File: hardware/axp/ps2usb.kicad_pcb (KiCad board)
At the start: 2 copper layers, 40 x 55 mm, 22 parts, among them J1 DIN8, J2 USB1035, J3 DIN8, J4 DB9_Female_MountingHoles, J5 Conn_01x03_Pin, U1 CH559L-less, U2 MAX232

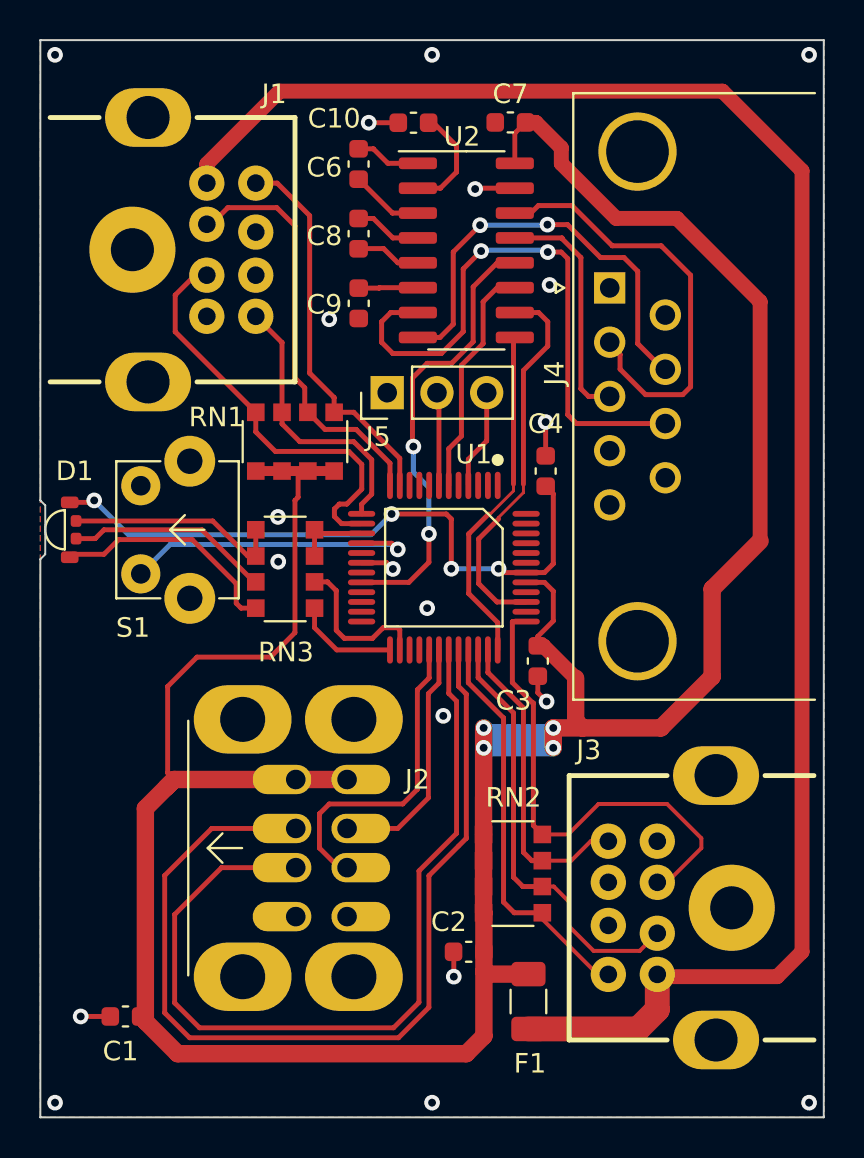
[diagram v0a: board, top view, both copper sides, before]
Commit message: Added crystal to PCB
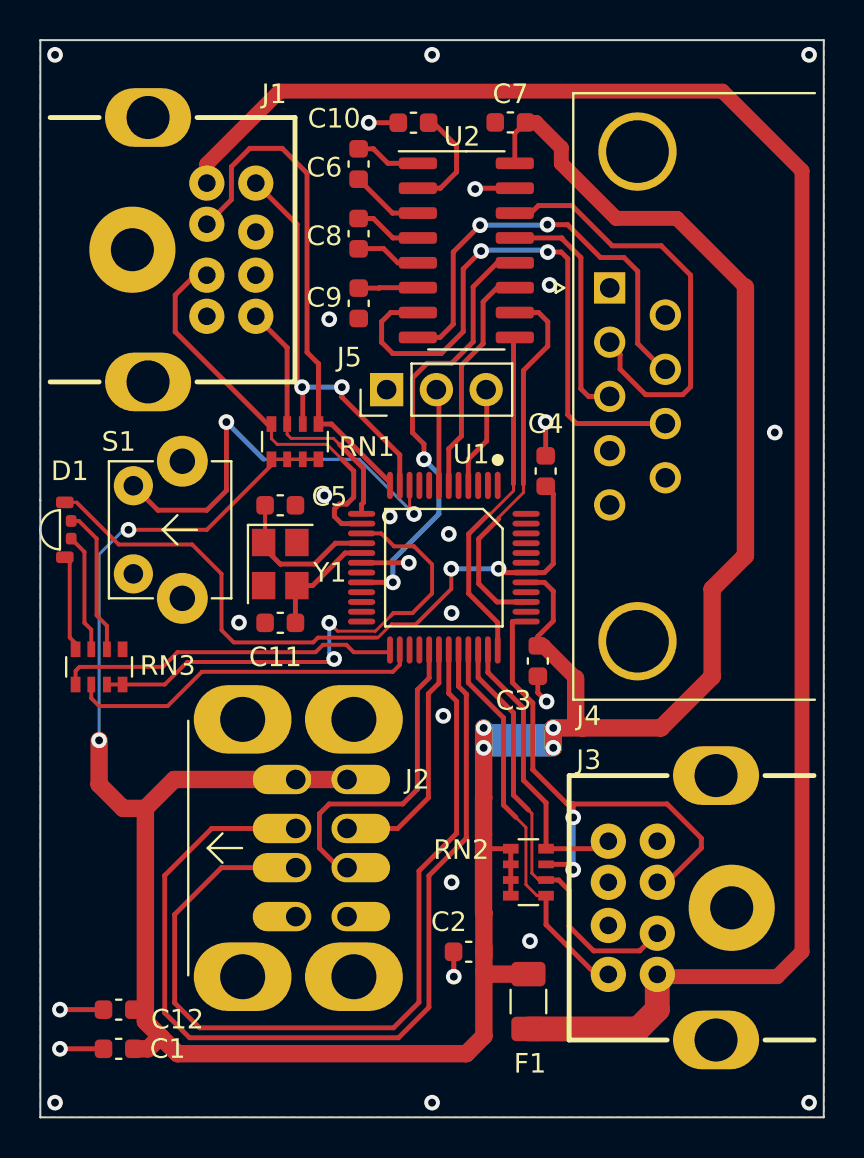
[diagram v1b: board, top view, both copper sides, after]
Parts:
- added C11: 10pF, Capacitor_SMD:C_0603_1608Metric, F.Cu at (109.2, 97.2)
- added C12: 3.3u, Capacitor_SMD:C_0603_1608Metric, F.Cu at (101.0, 119.0)
- added C5: 10pF, Capacitor_SMD:C_0603_1608Metric, F.Cu at (109.2, 91.2)
- added Y1: 12MHz, Crystal:Crystal_SMD_3225-4Pin_3.2x2.5mm, F.Cu at (109.2, 94.2)
- C10, C6, C7, C8, C9: value 1u -> 3.3u
- C3: value 100n -> 3.3u
- J4: value DB9_Female_MountingHoles -> DE9
- RN1, RN2, RN3: footprint Resistor_SMD:R_Array_Convex_4x1206 -> Resistor_SMD:R_Array_Convex_4x0603
- moved RN3 10.7 mm to (100.0, 99.5), turned to -90 degrees
- moved RN2 0.79 mm to (121.9, 110.0)
- moved C1 0.49 mm to (101.0, 117.0)
- moved S1 0.38 mm to (103.0, 92.5)
- moved D1 0.25 mm to (98.2, 92.5)
- moved J5 0.16 mm to (114.7, 85.3)
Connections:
- RN1 pad 1: /DIN1-8 -> /DIN1-2
- RN1 pad 2: /DIN1-2 -> /DIN1-8
- RN2 pad 3: /DIN2-6 -> /DIN2-1
- RN2 pad 4: /DIN2-1 -> /DIN2-6
- S1 pad 1: GND -> Net-(U1A-P3.4/LEDC/XCS0/T0)
- S1 pad 2: Net-(U1A-P4.6/XI/SCS_) -> GND
- U1 pad 10: (no net) -> Net-(U1A-P3.4/LEDC/XCS0/T0)
- U1 pad 17: (no net) -> Net-(U1A-P4.7/X0/SCK_)
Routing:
- net Net-(RN3-R1.2): track 3.99 -> 26.4 mm, vias 0 -> 2
- net Net-(U1A-P3.4/LEDC/XCS0/T0): track 0.00 -> 22.4 mm, vias 0 -> 2
- net Net-(RN3-R4.2): track 5.32 -> 17.3 mm
- net Net-(RN3-R3.2): track 8.03 -> 18.3 mm
- net Net-(U1A-P4.6/XI/SCS_): track 15.8 -> 7.98 mm, vias 1 -> 0
- net +5V: track 149.9 -> 157.2 mm, vias 4 -> 6
- net Net-(D1-R): track 11.9 -> 4.93 mm
- net Net-(U1A-P4.7/X0/SCK_): track 0.00 -> 5.92 mm
- net /DIN1-2: track 21.4 -> 26.5 mm
- net Net-(D1-G): track 10.5 -> 6.07 mm
- net Net-(D1-B): track 11.3 -> 7.54 mm
- net GND: track 12.8 -> 16.5 mm, vias 19 -> 25
- net +3.3V: track 32.9 -> 36.1 mm, vias 4 -> 2
- net /DIN2-1: track 25.2 -> 27.1 mm, vias 0 -> 2
- net /DIN1-8: track 19.7 -> 21.6 mm, vias 0 -> 2
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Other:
- outline, holes or cut-outs redrawn
- board text added: "AXP"
- board text added: "github:rasteri/HIDman"
- board text added: "rev c"
- board text removed: "rasteri.com"

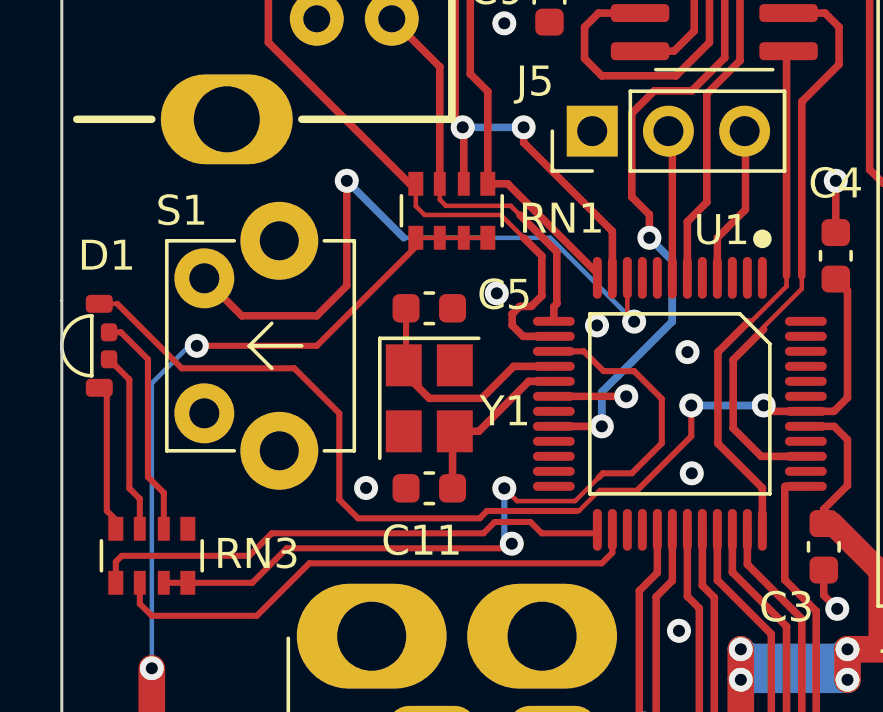
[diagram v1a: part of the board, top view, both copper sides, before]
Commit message: Software for new switch pin, refactoring, latest gerbers,
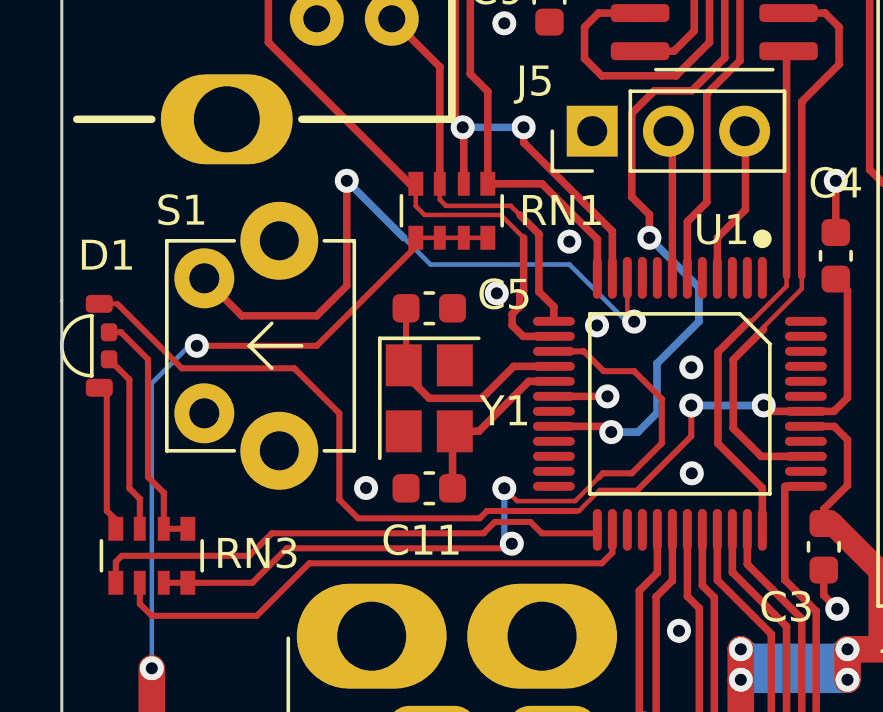
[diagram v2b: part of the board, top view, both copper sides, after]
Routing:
- net Net-(U1A-P4.0/LED2/A0/RXD1_): track 22.9 -> 24.6 mm
- net Net-(D1-B): track 7.54 -> 8.34 mm
- net /DIN1-1: track 21.3 -> 20.6 mm
- net /DIN1-2: track 26.5 -> 27.2 mm
- net GND: track 16.5 -> 15.9 mm, vias 25 -> 26
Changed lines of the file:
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@@
 		(tags "resistor array")
 		(property "Reference" "RN1"
-			(at 0.265 -3.665 0)
+			(at 0.011 -3.665 0)
 			(layer "F.SilkS")
 			(effects
@@
 	)
 	(segment
+		(start 115.189 94.185)
+		(end 113.402 94.185)
+		(width 0.25)
+		(layer "F.Cu")
+		(net 2)
+	)
+	(segment
 		(start 122.4 100.819142)
 		(end 122.4 99.975)
@@
 	)
 	(segment
-		(start 115.815 94.185)
-		(end 113.402 94.185)
-		(width 0.25)
-		(layer "F.Cu")
-		(net 2)
-	)
-	(segment
 		(start 118.097 115.329)
 		(end 118.11 115.316)
@@
 	)
 	(via
+		(at 113.919 89.027)
+		(size 0.8)
+		(drill 0.4)
+		(layers "F.Cu" "B.Cu")
+		(free yes)
+		(net 2)
+	)
+	(via
 		(at 122.848345 101.267487)
 		(size 0.8)
@@
 	)
 	(via
-		(at 117.856 92.71)
+		(at 117.983 93.218)
 		(size 0.8)
 		(drill 0.4)
@@
 	)
 	(via
-		(at 115.815 94.185)
+		(at 115.189 94.185)
 		(size 0.8)
 		(drill 0.4)
@@
 	)
 	(segment
-		(start 112.268 91.186)
-		(end 112.014 91.44)
+		(start 112.014 91.821)
+		(end 112.378 92.185)
 		(width 0.254)
 		(layer "F.Cu")
@@
 	)
 	(segment
-		(start 112.395 88.9)
-		(end 113 89.505)
+		(start 108.597326 87.1)
+		(end 108.8 87.1)
 		(width 0.254)
 		(layer "F.Cu")
@@
 	)
 	(segment
-		(start 113 89.505)
-		(end 113 90.835)
+		(start 112.014 91.44)
+		(end 112.014 91.821)
 		(width 0.254)
 		(layer "F.Cu")
@@
 	)
 	(segment
-		(start 112.649 91.186)
-		(end 112.268 91.186)
+		(start 112.268 91.186)
+		(end 112.014 91.44)
 		(width 0.254)
 		(layer "F.Cu")
@@
 	)
 	(segment
-		(start 108.597326 87.1)
-		(end 108.8 87.1)
+		(start 105.5625 78.8)
+		(end 105.14 78.8)
 		(width 0.254)
 		(layer "F.Cu")
@@
 	)
 	(segment
-		(start 105.5625 78.8)
-		(end 105.14 78.8)
+		(start 112.395 88.9)
+		(end 112.395 90.678)
 		(width 0.254)
 		(layer "F.Cu")
@@
 	)
 	(segment
-		(start 112.014 91.44)
-		(end 112.014 91.821)
-		(width 0.254)
+		(start 112.395 88.9)
+		(end 111.633 88.138)
+		(width 0.1524)
 		(layer "F.Cu")
 		(net 4)
 	)
 	(segment
-		(start 112.378 92.185)
-		(end 113.402 92.185)
+		(start 104.904 79.5)
+		(end 103.886 80.518)
 		(width 0.254)
 		(layer "F.Cu")
@@
 	)
 	(segment
-		(start 112.395 88.9)
-		(end 111.633 88.138)
-		(width 0.1524)
+		(start 112.395 90.678)
+		(end 112.268 90.805)
+		(width 0.254)
 		(layer "F.Cu")
 		(net 4)
 	)
 	(segment
-		(start 104.904 79.5)
-		(end 103.886 80.518)
+		(start 112.378 92.185)
+		(end 113.402 92.185)
 		(width 0.254)
 		(layer "F.Cu")
@@
 	)
 	(segment
-		(start 113 90.835)
-		(end 112.649 91.186)
+		(start 112.268 90.805)
+		(end 112.268 91.186)
 		(width 0.254)
 		(layer "F.Cu")
@@
 	)
 	(segment
-		(start 112.014 91.821)
-		(end 112.378 92.185)
-		(width 0.254)
-		(layer "F.Cu")
-		(net 4)
-	)
-	(segment
 		(start 106.755785 75.644215)
 		(end 105.5 76.9)
@@
 	)
 	(segment
+		(start 114.852 90.235)
+		(end 114.852 88.944)
+		(width 0.254)
+		(layer "F.Cu")
+		(net 5)
+	)
+	(segment
 		(start 110.617 83.439)
 		(end 110.617 74.295)
@@
 	)
 	(segment
-		(start 114.852 90.087)
-		(end 111.865 87.1)
+		(start 113.008 87.1)
+		(end 111.2 87.1)
 		(width 0.254)
 		(layer "F.Cu")
@@
 	)
 	(segment
-		(start 106.755785 73.965215)
-		(end 106.755785 75.644215)
+		(start 114.852 88.944)
+		(end 113.008 87.1)
 		(width 0.254)
 		(layer "F.Cu")
@@
 	)
 	(segment
-		(start 111.865 87.1)
-		(end 111.2 87.1)
+		(start 106.755785 73.965215)
+		(end 106.755785 75.644215)
 		(width 0.254)
 		(layer "F.Cu")
@@
 	)
 	(segment
-		(start 114.852 90.235)
-		(end 114.852 90.087)
+		(start 113.402 91.195)
+		(end 113.402 91.685)
 		(width 0.254)
 		(layer "F.Cu")
-		(net 5)
+		(net 6)
 	)
 	(segment
@@
 	)
 	(segment
-		(start 113.5 91.097)
-		(end 113.402 91.195)
+		(start 112.268 88.138)
+		(end 112.903 88.773)
 		(width 0.254)
 		(layer "F.Cu")
@@
 	)
 	(segment
-		(start 112.268 88.138)
-		(end 113.5 89.37)
-		(width 0.254)
-		(layer "F.Cu")
-		(net 6)
-	)
-	(segment
-		(start 113.5 89.37)
-		(end 113.5 91.097)
+		(start 109.6 83.2)
+		(end 108 81.6)
 		(width 0.254)
 		(layer "F.Cu")
@@
 	)
 	(segment
-		(start 109.6 83.2)
-		(end 108 81.6)
+		(start 112.903 90.696)
+		(end 113.402 91.195)
 		(width 0.254)
 		(layer "F.Cu")
@@
 	)
 	(segment
-		(start 113.402 91.195)
-		(end 113.402 91.685)
+		(start 109.6 87.1)
+		(end 109.6 83.2)
 		(width 0.254)
 		(layer "F.Cu")
@@
 	)
 	(segment
-		(start 109.6 87.1)
-		(end 109.6 83.2)
+		(start 112.903 88.773)
+		(end 112.903 90.696)
 		(width 0.254)
 		(layer "F.Cu")
@@
 	)
 	(segment
+		(start 100.4 98.6)
+		(end 101.2 98.6)
+		(width 0.2032)
+		(layer "F.Cu")
+		(net 22)
+	)
+	(segment
 		(start 99.25248 97.25248)
 		(end 99.25248 93.62748)
@@
 	)
 	(segment
-		(start 115 95.185)
-		(end 113.402 95.185)
+		(start 116.586 88.125183)
+		(end 116 87.539183)
 		(width 0.254)
 		(layer "F.Cu")
@@
 	)
 	(segment
-		(start 116.586 88.125183)
-		(end 116 87.539183)
+		(start 116 87.539183)
+		(end 116 84.75)
 		(width 0.254)
 		(layer "F.Cu")
@@
 	)
 	(segment
-		(start 116 87.539183)
-		(end 116 84.75)
+		(start 115.316 95.377)
+		(end 115.124 95.185)
 		(width 0.254)
 		(layer "F.Cu")
@@
 	)
 	(segment
+		(start 115.124 95.185)
+		(end 113.402 95.185)
+		(width 0.254)
+		(layer "F.Cu")
+		(net 44)
+	)
+	(segment
 		(start 119.098 82.902)
 		(end 119.098 80.0978)
@@
 	)
 	(via
-		(at 115 95.185)
+		(at 115.316 95.377)
 		(size 0.8)
 		(drill 0.4)
@@
 	)
 	(segment
-		(start 115 94.039183)
-		(end 115 95.185)
+		(start 116.205 95.377)
+		(end 116.84 94.742)
 		(width 0.254)
 		(layer "B.Cu")
@@
 	)
 	(segment
-		(start 117.348 91.694)
-		(end 115.5364 93.5056)
+		(start 118.237 90.551)
+		(end 116.586 88.9)
 		(width 0.254)
 		(layer "B.Cu")
@@
 	)
 	(segment
-		(start 115.5364 93.5056)
-		(end 115.533583 93.5056)
+		(start 116.84 94.742)
+		(end 116.84 93.091)
 		(width 0.254)
 		(layer "B.Cu")
@@
 	)
 	(segment
-		(start 117.348 89.662)
-		(end 117.348 91.694)
+		(start 116.84 93.091)
+		(end 118.237 91.694)
 		(width 0.254)
 		(layer "B.Cu")
@@
 	)
 	(segment
-		(start 115.533583 93.5056)
-		(end 115 94.039183)
+		(start 115.316 95.377)
+		(end 116.205 95.377)
 		(width 0.254)
 		(layer "B.Cu")
@@
 	)
 	(segment
-		(start 116.586 88.9)
-		(end 117.348 89.662)
+		(start 118.237 91.694)
+		(end 118.237 90.551)
 		(width 0.254)
 		(layer "B.Cu")
@@
 	)
 	(segment
+		(start 113.919 89.789)
+		(end 115.824 91.694)
+		(width 0.1524)
+		(layer "B.Cu")
+		(net 49)
+	)
+	(segment
 		(start 108.4 88.9)
-		(end 113.284 88.9)
+		(end 106.5 87)
+		(width 0.25)
+		(layer "B.Cu")
+		(net 49)
+	)
+	(segment
+		(start 108.4 88.9)
+		(end 109.289 89.789)
 		(width 0.1524)
 		(layer "B.Cu")
@@
 	)
 	(segment
-		(start 113.284 88.9)
-		(end 116.078 91.694)
+		(start 109.289 89.789)
+		(end 113.919 89.789)
 		(width 0.1524)
 		(layer "B.Cu")
@@
 	)
 	(segment
-		(start 108.4 88.9)
-		(end 106.5 87)
-		(width 0.25)
+		(start 115.824 91.694)
+		(end 116.078 91.694)
+		(width 0.1524)
 		(layer "B.Cu")
 		(net 49)

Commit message: redundant code cleanup
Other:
- board text added: "rev d"
- board text removed: "rev c"
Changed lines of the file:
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@@
 		(at 98.25 92.5 180)
 		(property "Reference" "D1"
-			(at -0.25 3 0)
+			(at -0.25 -3 0)
 			(unlocked yes)
 			(layer "F.SilkS")
@@
 		)
 		(property "Value" "Conn_01x03_Pin"
-			(at 0 7.41 270)
+			(at 0 7.41 -90)
 			(layer "F.Fab")
 			(effects
@@
 		)
 		(fp_text user "${REFERENCE}"
-			(at 0 2.54 360)
+			(at 0 2.54 0)
 			(layer "F.Fab")
 			(effects
@@
 		(layer "B.SilkS")
 	)
+	(gr_circle
+		(center 99.271176 91.183159)
+		(end 99.424647 91.233822)
+		(stroke
+			(width 0.3)
+			(type default)
+		)
+		(fill none)
+		(layer "F.SilkS")
+	)
 	(gr_poly
 		(pts
@@
 		)
 	)
-	(gr_text "rev c"
+	(gr_text "rev d"
 		(at 118 79.5 0)
 		(layer "B.SilkS")
@@
 	)
 	(segment
-		(start 130.75 108.75)
-		(end 129 110.5)
+		(start 124.206 107.188)
+		(end 124.206 106.5)
 		(width 0.254)
 		(layer "F.Cu")
@@
 	)
 	(segment
-		(start 124.206 107.188)
-		(end 124.206 106.5)
+		(start 130.5 108)
+		(end 130.5 109)
 		(width 0.254)
 		(layer "F.Cu")
@@
 	)
 	(segment
-		(start 121.1 100.3)
-		(end 122.146 101.346)
+		(start 129 106.5)
+		(end 130.5 108)
 		(width 0.254)
 		(layer "F.Cu")
@@
 	)
 	(segment
-		(start 124.206 106.5)
-		(end 129 106.5)
+		(start 121.1 100.3)
+		(end 122.146 101.346)
 		(width 0.254)
 		(layer "F.Cu")
@@
 	)
 	(segment
-		(start 130.75 108.25)
-		(end 130.75 108.75)
+		(start 124.206 106.5)
+		(end 129 106.5)
 		(width 0.254)
 		(layer "F.Cu")
@@
 	)
 	(segment
+		(start 130.5 109)
+		(end 129 110.5)
+		(width 0.254)
+		(layer "F.Cu")
+		(net 8)
+	)
+	(segment
 		(start 121.802 97.185)
 		(end 121.115 97.185)
@@
 		(width 0.254)
 		(layer "F.Cu")
-		(net 8)
-	)
-	(segment
-		(start 129 106.5)
-		(end 130.75 108.25)
-		(width 0.254)
-		(layer "F.Cu")

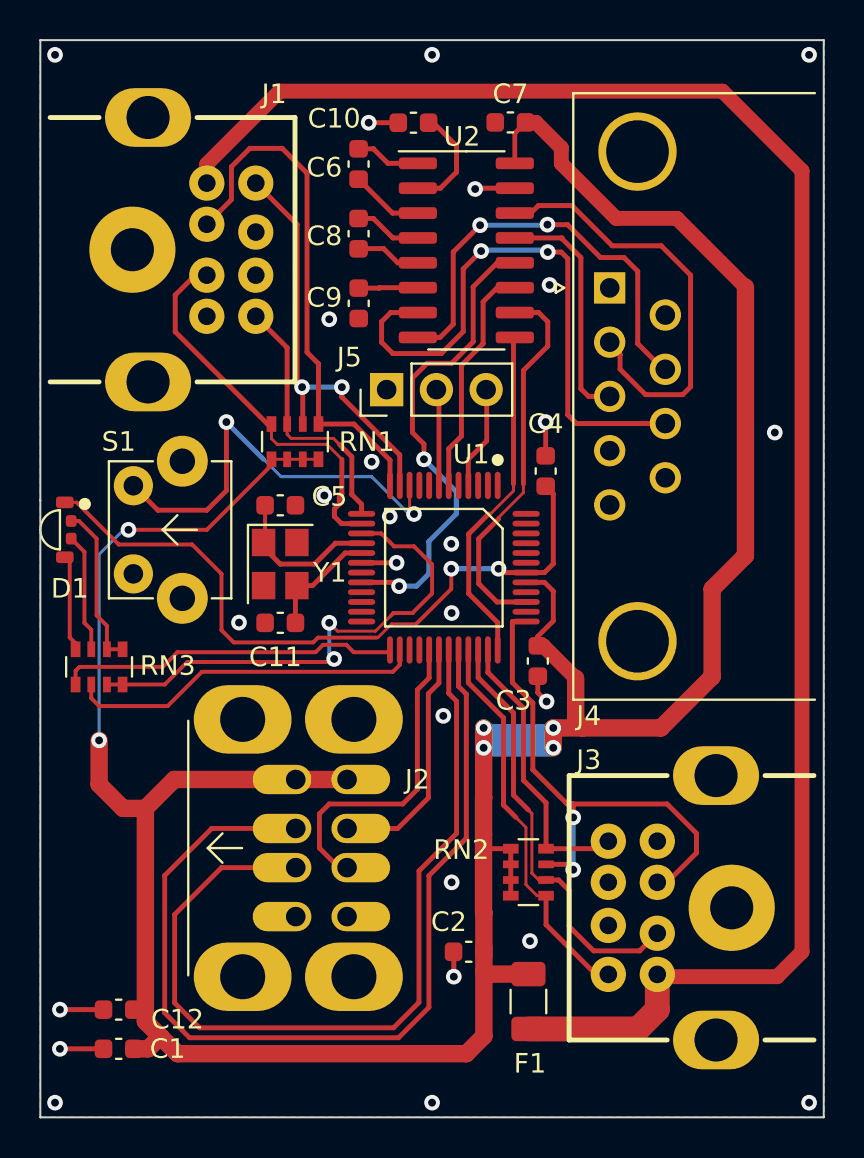
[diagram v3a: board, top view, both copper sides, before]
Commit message: moved some capacitors around
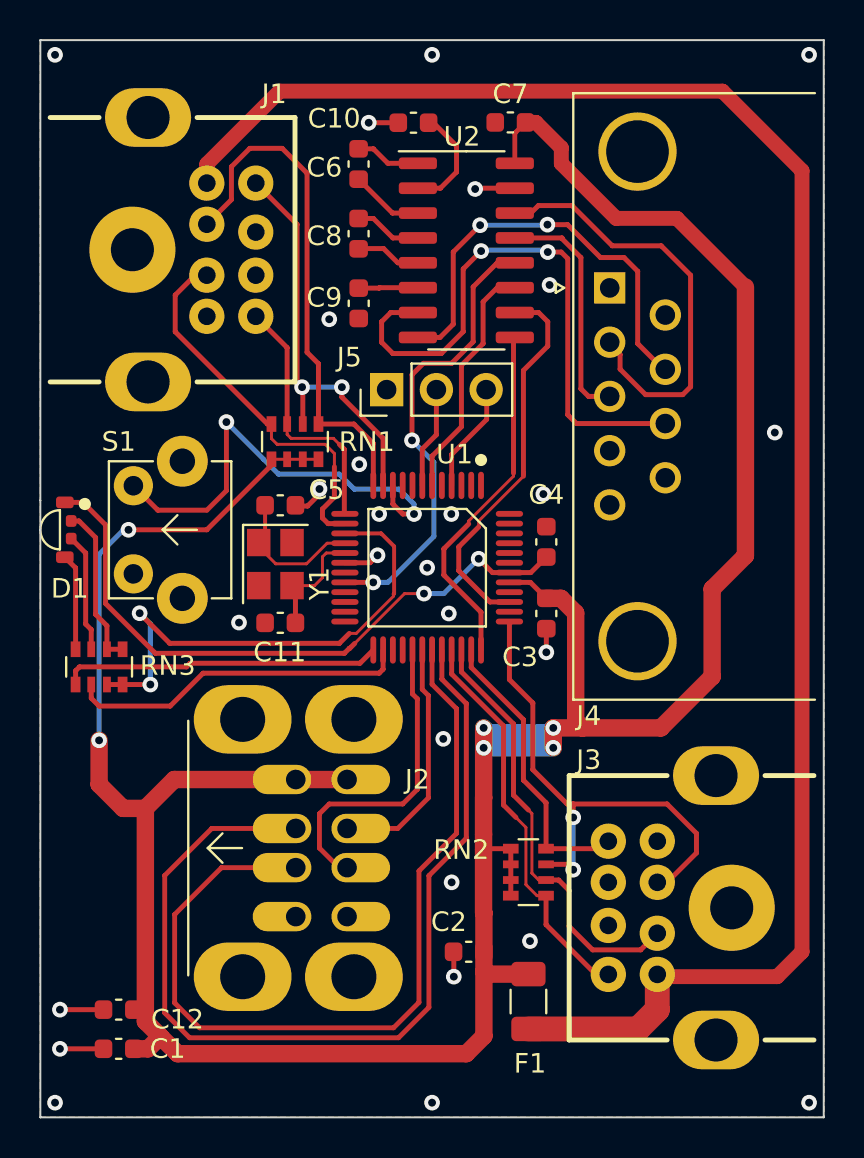
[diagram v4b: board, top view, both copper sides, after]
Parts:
- moved C4 3.62 mm to (122.8, 93.1)
- moved C3 2.46 mm to (122.8, 96.8)
- moved U1 0.85 mm to (116.8, 94.4)
- moved Y1 0.25 mm to (109.0, 94.2)
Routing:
- net +3.3V: track 36.1 -> 32.7 mm
- net Net-(U1A-P3.4/LEDC/XCS0/T0): track 22.4 -> 23.7 mm
- net Net-(RN3-R4.2): track 17.3 -> 16.1 mm
- net Net-(U1A-P4.0/LED2/A0/RXD1_): track 24.6 -> 23.5 mm
- net Net-(J5-Pin_2): track 4.53 -> 5.33 mm
- net Net-(RN3-R3.2): track 18.3 -> 17.5 mm
- net Net-(U1A-P0.4/AD4/UCTS): track 17.6 -> 18.2 mm
- net Net-(U1A-P4.6/XI/SCS_): track 7.98 -> 7.35 mm
- net /DIN2-1: track 26.9 -> 26.3 mm
- net GND: track 15.9 -> 15.7 mm, vias 26 -> 27
